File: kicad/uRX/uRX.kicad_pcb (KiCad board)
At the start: 2 copper layers, 13 x 1.4 mm, 118 parts, among them J1 RF_GMD, J2 C165948, J3 AudioJack2_Ground, J4 +5Vfiltered, J5 +5V, J6 U.FL, J7 +3.3Vfiltered, J8 RF_In, J9 RF_In, Q1 BC847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

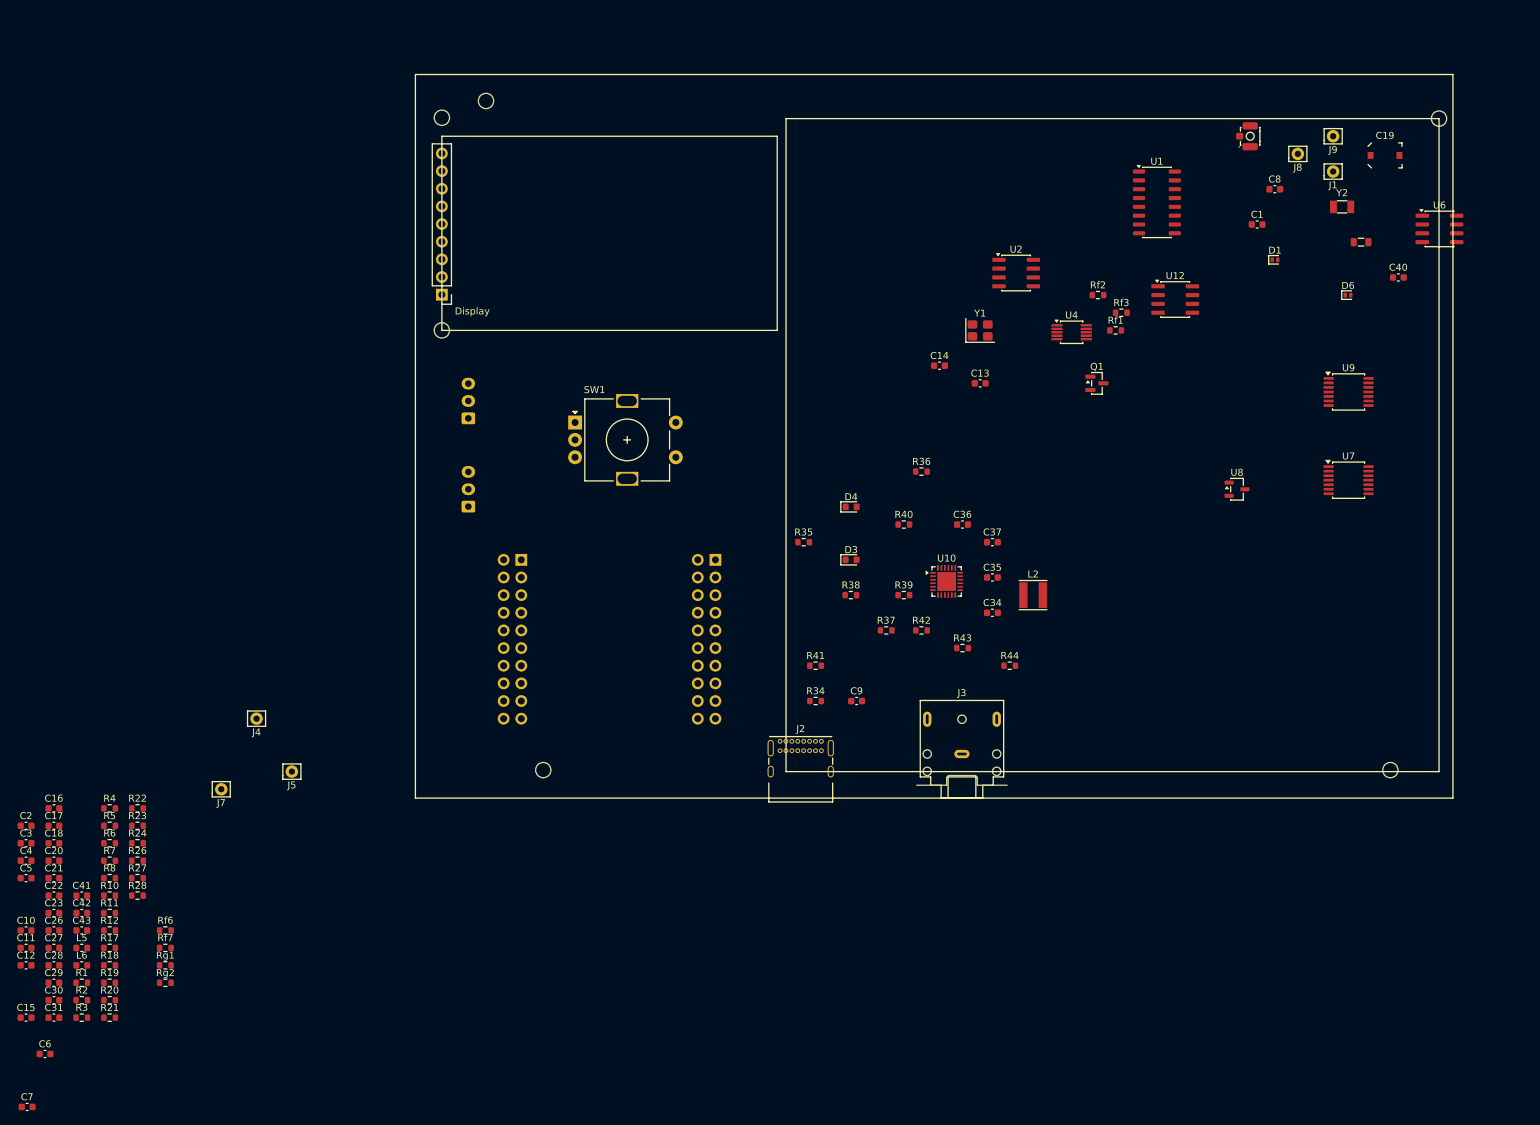
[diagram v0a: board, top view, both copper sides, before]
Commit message: add esp32 to pcb
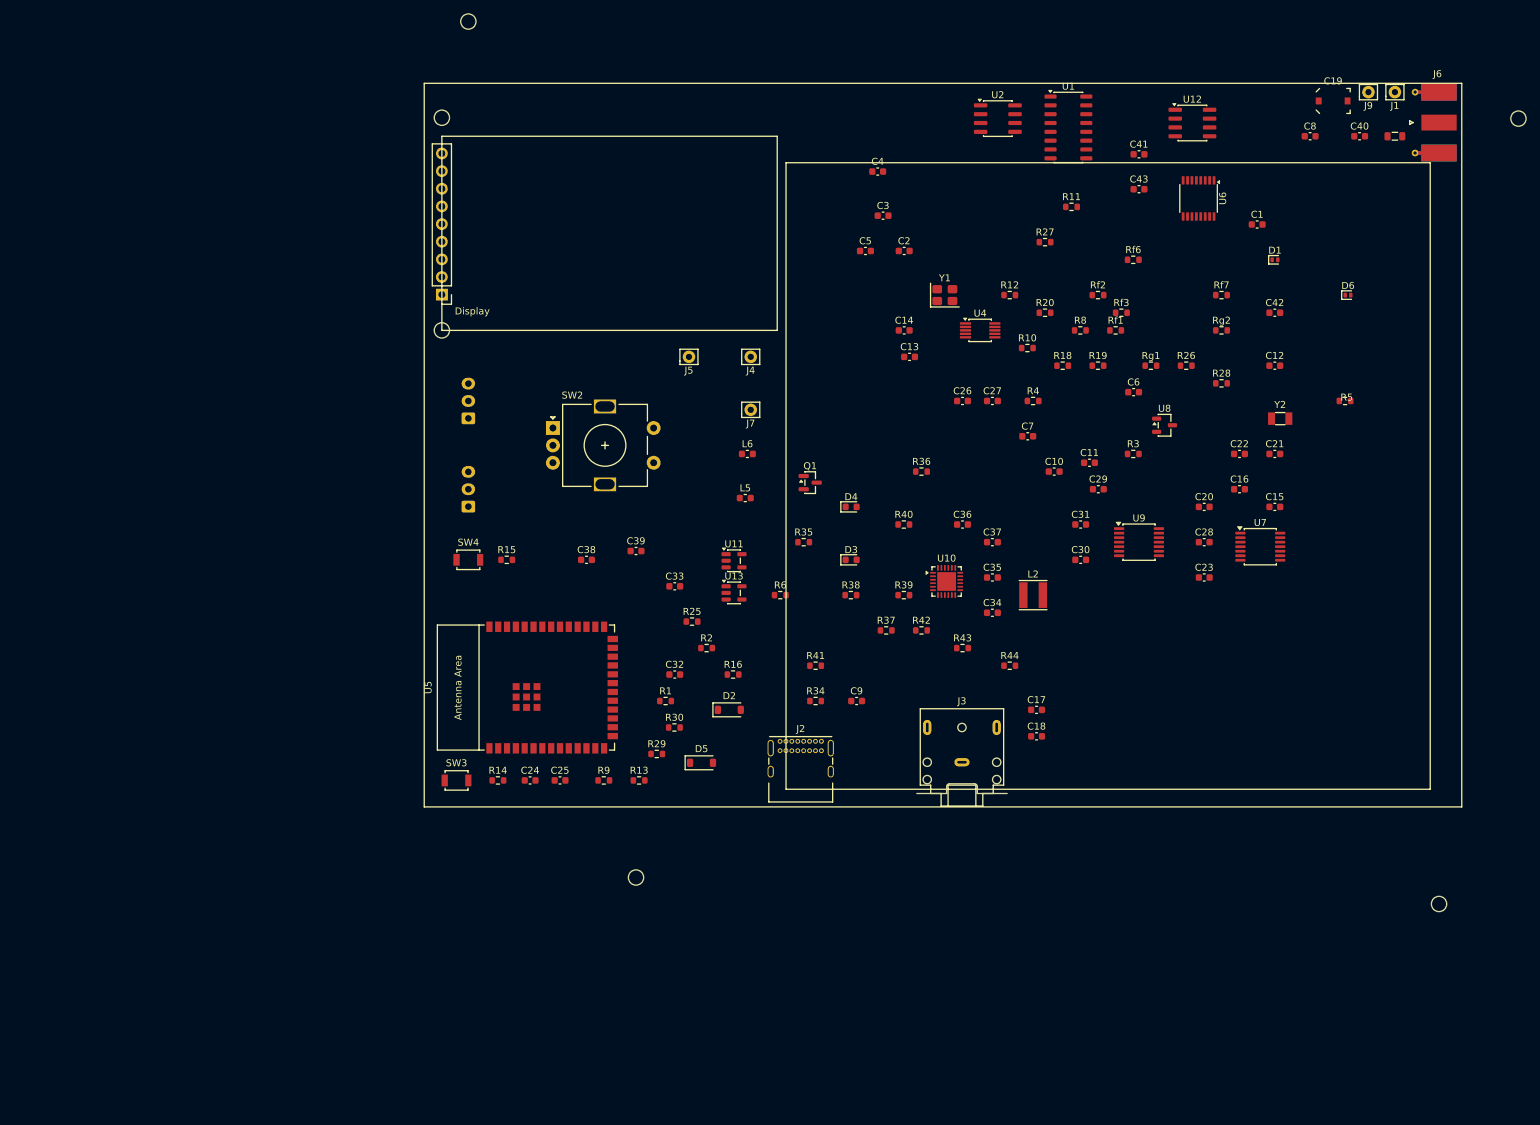
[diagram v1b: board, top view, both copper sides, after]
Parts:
- removed J8: RF_In, Connector_Pin:Pin_D0.9mm_L10.0mm_W2.4mm_FlatFork
- removed R17, R7: 4.7kΩ, Resistor_SMD:R_0603_1608Metric
- removed R21, R22, R23, R24: 22, Resistor_SMD:R_0603_1608Metric
- removed REF** (x2): HDGCPH2.54‑PZS‑2X10, Connector_PinHeader_2.54mm:PinHeader_2x10_P2.54mm_Vertical
- removed SW1: RotaryEncoder_Switch, Rotary_Encoder:RotaryEncoder_Alps_EC11E-Switch_Vertical_H20mm
- added C24: 1u, Capacitor_SMD:C_0603_1608Metric, F.Cu at (95.2, 133.3)
- added C25: 47u, Capacitor_SMD:C_0603_1608Metric, F.Cu at (99.6, 133.3)
- added C32: 10n, Capacitor_SMD:C_0603_1608Metric, F.Cu at (116.1, 118.1)
- added C33: 100n, Capacitor_SMD:C_0603_1608Metric, F.Cu at (116.1, 105.4)
- added C38: 100n, Capacitor_SMD:C_0603_1608Metric, F.Cu at (103.4, 101.6)
- added C39: 100n, Capacitor_SMD:C_0603_1608Metric, F.Cu at (110.5, 100.3)
- added D2: D_Schottky, Diode_SMD:D_SOD-123, F.Cu at (123.9, 123.2)
- added D5: D_Schottky, Diode_SMD:D_SOD-123, F.Cu at (119.9, 130.8)
- added R13: 4.7K, Resistor_SMD:R_0603_1608Metric, F.Cu at (110.9, 133.3)
- added R14: 10k, Resistor_SMD:R_0603_1608Metric, F.Cu at (90.6, 133.3)
- added R15: 10k, Resistor_SMD:R_0603_1608Metric, F.Cu at (91.9, 101.6)
- added R16: 22, Resistor_SMD:R_0603_1608Metric, F.Cu at (124.5, 118.1)
- added R25: 22, Resistor_SMD:R_0603_1608Metric, F.Cu at (118.6, 110.5)
- added R29: 22, Resistor_SMD:R_0603_1608Metric, F.Cu at (113.5, 129.5)
- added R30: 22, Resistor_SMD:R_0603_1608Metric, F.Cu at (116.0, 125.7)
- added R9: 4.7K, Resistor_SMD:R_0603_1608Metric, F.Cu at (105.9, 133.3)
- added SW2: RotaryEncoder_Switch, Rotary_Encoder:RotaryEncoder_Alps_EC11E-Switch_Vertical_H20mm, F.Cu at (98.5, 82.6)
- added SW3: Reset, Button_Switch_SMD:SW_SPST_B3U-1000P, F.Cu at (84.7, 133.3)
- added SW4: Boot, Button_Switch_SMD:SW_SPST_B3U-1000P, F.Cu at (86.4, 101.6)
- added U11: LP2985-5.0, Package_TO_SOT_SMD:SOT-23-5, F.Cu at (124.6, 101.7)
- added U13: HT733333, Package_TO_SOT_SMD:SOT-23-5, F.Cu at (124.6, 106.4)
- added U5: ESP32-S3-WROOM-2, PCM_Espressif:ESP32-S3-WROOM-2, F.Cu at (97.7, 120.0)
- J1: value RF_GMD -> RF_AM_GND
- J6: footprint PCM_JLCPCB:IPEX-SMD_BWIPX-1-001E -> Connector_Coaxial:SMA_Molex_73251-1153_EdgeMount_Horizontal
- J9: value RF_In -> RF_AM__In
- U6: footprint Package_SO:SOIC-8_3.9x4.9mm_P1.27mm -> Package_SO:SSOP-16_3.9x4.9mm_P0.635mm
- moved C12 199.4 mm to (202.4, 73.7)
- moved C15 194.2 mm to (202.4, 94.0)
- moved C42 192.2 mm to (202.4, 66.0)
- moved R5 188.0 mm to (212.5, 78.7)
- moved C21 186.0 mm to (202.4, 86.4)
- moved C41 185.8 mm to (182.9, 43.2)
- moved C43 185.8 mm to (182.9, 48.3)
- moved C6 183.3 mm to (182.1, 77.5)
- moved C22 182.1 mm to (197.3, 86.4)
- moved Rf7 178.7 mm to (194.8, 63.5)
- moved Rg2 178.7 mm to (194.8, 68.6)
- moved C16 176.7 mm to (197.3, 91.4)
- moved C28 176.4 mm to (192.3, 99.1)
- moved C7 173.4 mm to (166.9, 83.8)
- moved C20 173.2 mm to (192.3, 94.0)
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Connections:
- net Net-(U7-SCKI) renamed ADC_SCKI
- C10 pad 2: +5Vfiltered -> GND
- C11 pad 2: +5Vfiltered -> GND
- C13 pad 2: +5Vfiltered -> GND
- C14 pad 2: +5Vfiltered -> GND
- C19 pad 1: +5Vfiltered -> GND
- C2 pad 2: +5Vfiltered -> GND
- C20 pad 1: +5Vfiltered -> GND
- C21 pad 1: +5Vfiltered -> GND
- C22 pad 1: +5Vfiltered -> GND
- C23 pad 1: +5Vfiltered -> GND
- C26 pad 2: +5Vfiltered -> GND
- C27 pad 2: +5Vfiltered -> GND
- C28 pad 1: +5Vfiltered -> GND
- C29 pad 1: +5Vfiltered -> GND
- C3 pad 2: +5Vfiltered -> GND
- C30 pad 1: +5Vfiltered -> GND
- C31 pad 1: +5Vfiltered -> GND
- C34 pad 1: Net-(U10-EN) -> VBUS
- C34 pad 2: +5Vfiltered -> GND
- C36 pad 2: +5Vfiltered -> GND
- C37 pad 2: +5Vfiltered -> GND
- C4 pad 2: +5Vfiltered -> GND
- C40 pad 2: +5Vfiltered -> GND
- C41 pad 2: +5Vfiltered -> GND
- C43 pad 2: +5Vfiltered -> GND
- C5 pad 2: +5Vfiltered -> GND
- C8 pad 2: +5Vfiltered -> GND
- C9 pad 2: +5Vfiltered -> GND
- D3 pad 1: +5Vfiltered -> GND
- D4 pad 1: +5Vfiltered -> GND
- D6 pad 2: +5Vfiltered -> GND
- J1 pad 1: +5Vfiltered -> GND
- J2 pad A1: +5Vfiltered -> GND
- J2 pad A12: +5Vfiltered -> GND
- J2 pad A4: Net-(U10-EN) -> VBUS
- J2 pad A6: Net-(U10-DP) -> USB_D+
- J2 pad A7: Net-(U10-DM) -> USB_D-
- J2 pad A9: Net-(U10-EN) -> VBUS
- J2 pad B1: +5Vfiltered -> GND
- J2 pad B12: +5Vfiltered -> GND
- J2 pad B4: Net-(U10-EN) -> VBUS
- J2 pad B6: Net-(U10-DP) -> USB_D+
- J2 pad B7: Net-(U10-DM) -> USB_D-
- J2 pad B9: Net-(U10-EN) -> VBUS
- J6 pad 2: +5Vfiltered -> GND
- L2 pad 2: Net-(U10-EN) -> VBUS
- R1 pad 1: Net-(U7-LRCK) -> /I2S_BCK
- R1 pad 2: /I2S0_LRCK -> Net-(U5-GPIO11/TOUCH11/ADC2_CH0/FSPID/FSPIIO5/SUBSPID)
- R2 pad 1: Net-(U7-BCK) -> /I2S_LRCK
- R2 pad 2: /I2S0_BCK -> Net-(U5-GPIO12/TOUCH12/ADC2_CH1/FSPICLK/FSPIIO6/SUBSPICLK)
- R34 pad 2: +5Vfiltered -> GND
- R35 pad 2: +5Vfiltered -> GND
- R36 pad 2: +5Vfiltered -> GND
- R37 pad 2: +5Vfiltered -> GND
- R41 pad 2: +5Vfiltered -> GND
- R42 pad 2: +5Vfiltered -> GND
- R43 pad 2: +5Vfiltered -> GND
- R44 pad 1: Net-(U10-EN) -> VBUS
- R44 pad 2: +5Vfiltered -> GND
- R5 pad 2: Net-(U3-D33) -> RST_4732
- U12 pad 4: +5Vfiltered -> GND
- U7 pad 10: +5Vfiltered -> GND
- U7 pad 11: +5Vfiltered -> GND
- U7 pad 12: +5Vfiltered -> GND
- U7 pad 2: +5Vfiltered -> GND
- U7 pad 5: +5Vfiltered -> GND
- U7 pad 7: Net-(U7-LRCK) -> /I2S_LRCK
- U7 pad 8: Net-(U7-BCK) -> /I2S_BCK
- U7 pad 9: Net-(U7-DOUT) -> /I2S0_DOUT
- U9 pad 10: +5Vfiltered -> GND
- U9 pad 11: +5Vfiltered -> GND
- U9 pad 12: +5Vfiltered -> GND
- U9 pad 2: +5Vfiltered -> GND
- U9 pad 5: +5Vfiltered -> GND
- U9 pad 7: Net-(U9-LRCK) -> /I2S_LRCK
- U9 pad 8: Net-(U9-BCK) -> /I2S_BCK
- U9 pad 9: Net-(U9-DOUT) -> /I2S1_DOUT

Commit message: work on rf frontend and battery charger
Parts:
- removed C33, C38, C39: 100n, Capacitor_SMD:C_0603_1608Metric
- removed SW2: RotaryEncoder_Switch, Rotary_Encoder:RotaryEncoder_Alps_EC11E-Switch_Vertical_H20mm
- added C44: 100n, Capacitor_SMD:C_0603_1608Metric, F.Cu at (113.0, 91.5)
- added C45: 100n, Capacitor_SMD:C_0603_1608Metric, F.Cu at (93.5, 85.8)
- added C46: 100n, Capacitor_SMD:C_0603_1608Metric, F.Cu at (93.5, 97.0)
- added J5: +5V, Connector_Pin:Pin_D0.9mm_L10.0mm_W2.4mm_FlatFork, F.Cu at (120.8, 81.8)
- added J5: GND, Connector_Pin:Pin_D0.9mm_L10.0mm_W2.4mm_FlatFork, F.Cu at (109.5, 81.8)
- added J5: Bat, Connector_Pin:Pin_D0.9mm_L10.0mm_W2.4mm_FlatFork, F.Cu at (103.5, 81.8)
- added M2: , MountingHole:MountingHole_2.2mm_M2_DIN965, F.Cu at (259.8, -0.25)
- added SW1: RotaryEncoder_Switch, Rotary_Encoder:RotaryEncoder_Alps_EC11E-Switch_Vertical_H20mm, F.Cu at (96.0, 89.0)
- Bat2, Bat3: moved to F.Cu
- moved C3 84.8 mm to (222.7, 88.4), turned to -90 degrees
- moved U2 83.1 mm to (218.4, 99.6)
- moved C4 82.8 mm to (216.2, 88.4), turned to -90 degrees
- moved C5 82.1 mm to (219.4, 88.4), turned to -90 degrees
- moved C2 71.1 mm to (212.9, 88.4), turned to -90 degrees
- moved U1 62.5 mm to (219.6, 80.7), turned to -90 degrees
- moved R12 59.4 mm to (217.8, 89.1), turned to 90 degrees
- moved R10 57.1 mm to (221.1, 89.1), turned to 90 degrees
- moved R11 56.4 mm to (214.6, 89.1), turned to 90 degrees
- moved R8 53.9 mm to (224.2, 89.1), turned to 90 degrees
- moved C26 52.1 mm to (205.5, 58.5), turned to 90 degrees
- moved R27 50.7 mm to (216.4, 74.6), turned to 90 degrees
- moved C27 50.5 mm to (208.0, 58.5), turned to 90 degrees
- moved C41 47.4 mm to (220.4, 72.1), turned to 180 degrees
- moved C43 43.6 mm to (220.4, 70.4), turned to 180 degrees
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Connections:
- Bat2 pad 3: +5V -> +VBatt
- Bat3 pad 3: +5V -> +VBatt
- Q1 pad 3: Net-(Q1-C) -> Q_BAT_STAT
- U10 pad 1: Net-(U10-DM) -> unconnected-(U10-DM-Pad1)
- U10 pad 12: Net-(U10-EN) -> VBUS
- U10 pad 13: Net-(U10-EN) -> VBUS
- U10 pad 2: Net-(U10-DP) -> unconnected-(U10-DP-Pad2)
- U10 pad 21: +5V -> +VBatt
- U10 pad 22: +5V -> +VBatt
- U5 pad 25: unconnected-(U5-GPIO48/SPICLK_N/SUBSPICLK_N_DIFF-Pad25) -> Q_BAT_STAT
- U5 pad 31: unconnected-(U5-GPIO38/FSPIWP/SUBSPIWP-Pad31) -> Net-(U5-GPIO38/FSPIWP/SUBSPIWP)
- U5 pad 32: unconnected-(U5-MTCK/GPIO39/CLK_OUT3/SUBSPICS1-Pad32) -> Net-(U5-MTCK/GPIO39/CLK_OUT3/SUBSPICS1)
- U5 pad 33: unconnected-(U5-MTDO/GPIO40/CLK_OUT2-Pad33) -> Net-(U5-MTDO/GPIO40/CLK_OUT2)
- U5 pad 39: Q_BAT_STAT -> unconnected-(U5-GPIO1/TOUCH1/ADC1_CH0-Pad39)
- U5 pad 4: Net-(U5-GPIO4/TOUCH4/ADC1_CH3) -> unconnected-(U5-GPIO4/TOUCH4/ADC1_CH3-Pad4)
- U5 pad 5: Net-(U5-GPIO5/TOUCH5/ADC1_CH4) -> unconnected-(U5-GPIO5/TOUCH5/ADC1_CH4-Pad5)
- U5 pad 6: Net-(U5-GPIO6/TOUCH6/ADC1_CH5) -> unconnected-(U5-GPIO6/TOUCH6/ADC1_CH5-Pad6)
- U8 pad 1: (no net) -> /VRev2.5
- U8 pad 2: (no net) -> GND
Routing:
- net GND: track 0.00 -> 181.3 mm, vias 0 -> 12
- net +VBatt: track 0.00 -> 58.7 mm
- net Net-(U5-MTCK/GPIO39/CLK_OUT3/SUBSPICS1): track 0.00 -> 28.9 mm
- net +5V: track 0.00 -> 26.3 mm
- net Net-(U5-GPIO38/FSPIWP/SUBSPIWP): track 0.00 -> 24.8 mm
- net +5Vfiltered: track 0.00 -> 24.6 mm
- net Net-(U5-MTDO/GPIO40/CLK_OUT2): track 0.00 -> 21.9 mm
- net +3.3V: track 0.00 -> 17.7 mm
- net /VRev2.5: track 0.00 -> 15.7 mm
- net Net-(U1-1B1): track 0.00 -> 13.3 mm
- net Net-(Rf6-Pad2): track 0.00 -> 13.0 mm
- net Net-(U1-1B4): track 0.00 -> 12.9 mm
- net Net-(U1-1B2): track 0.00 -> 12.6 mm
- net Net-(U1-1B3): track 0.00 -> 12.1 mm
- net Net-(D2-K): track 0.00 -> 11.6 mm
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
